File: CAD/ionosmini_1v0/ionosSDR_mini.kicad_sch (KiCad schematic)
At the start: 8 parts, among them CON1 TFC-120-02-F-D-A-K-TR, CON2 TFC-120-02-F-D-A-K-TR, IC1 ESP32-S3-DEVKITC-1-N8R2, SW1 PTS647SK38SMTR2 LFS, SW2 PTS647SK38SMTR2 LFS, SW3 PTS647SK38SMTR2 LFS, SW4 PTS647SK38SMTR2 LFS

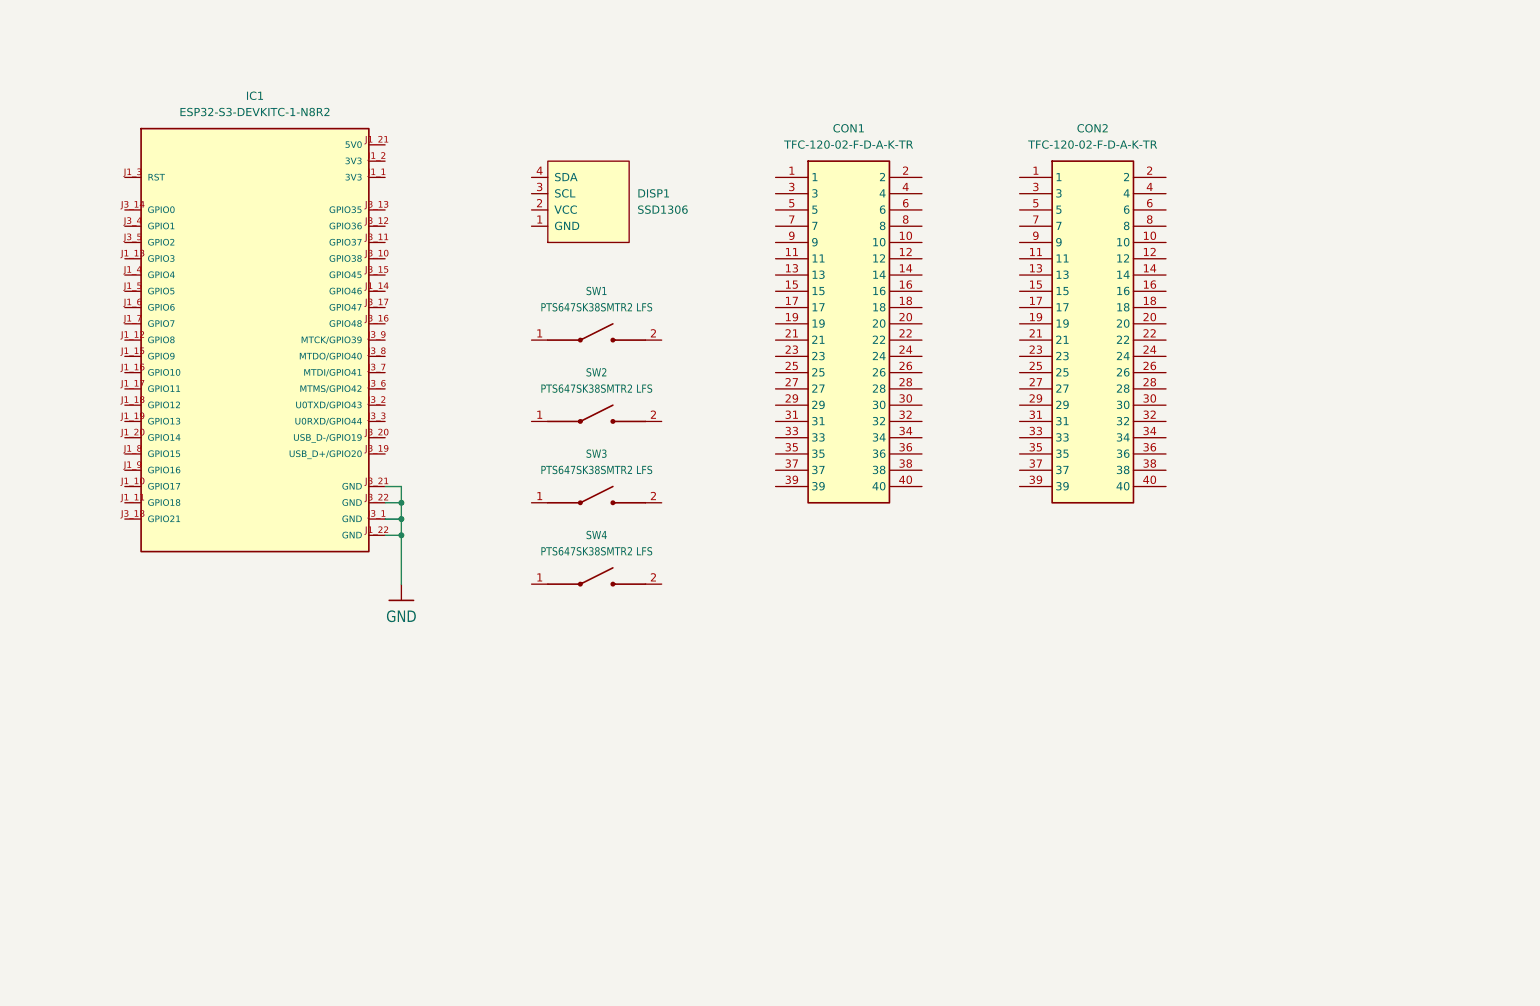
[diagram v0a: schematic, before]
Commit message: Pairing nets to ESP32
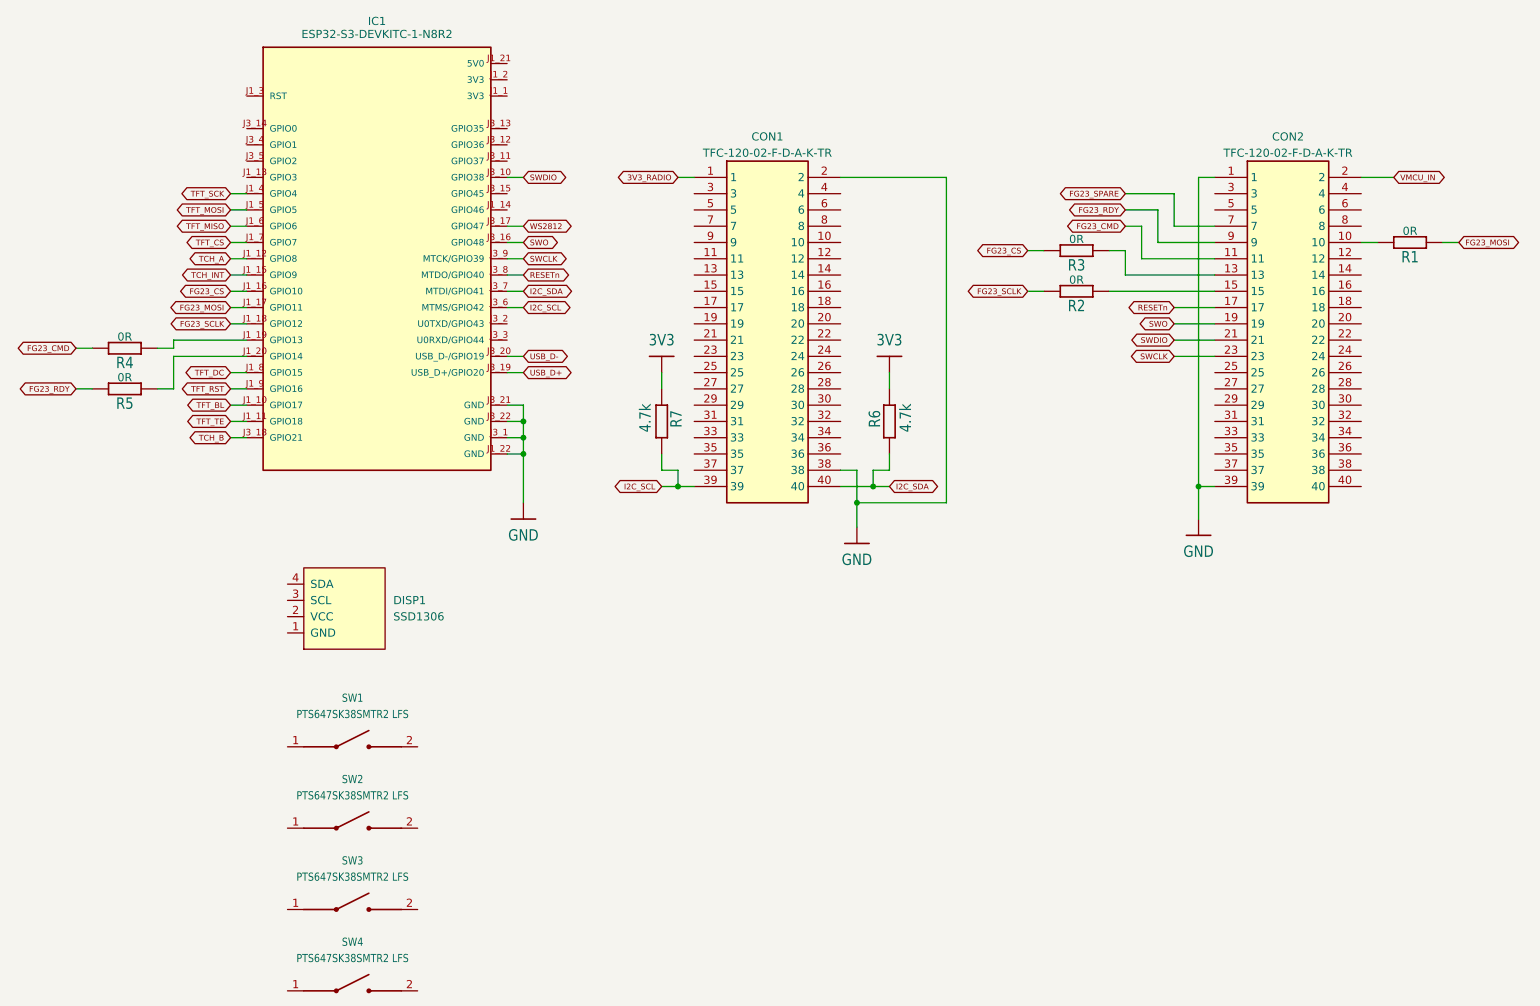
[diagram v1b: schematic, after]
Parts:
- added R1, R2, R3, R4, R5: 0R, rpw_lib:RESC1005X40_0402, symbol rpw_resistors:R_0R_JUMPER_0402(1005-METRIC)
- added R6, R7: 4.7k, rpw_lib:RESC1005X40_0402, symbol rpw_resistors:R_4.7K_5%_0402(1005-METRIC)
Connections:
- net GND: now also CON1.2, CON1.38, CON2.1, CON2.39
- net at CON2.10: now also R1.1
- net FG23_CMD: now reaches CON2.11
- net FG23_CMD: now also R4.1
- net at CON2.13: now also R3.2
- net at CON2.15: now also R2.2
- net RESETn: now reaches CON2.17
- net RESETn: now also IC1.J3_8 (MTDO/GPIO40)
- net SWO: now reaches CON2.19
- net SWO: now also IC1.J3_16 (GPIO48)
- net VMCU_IN: now reaches CON2.2
- net SWDIO: now reaches CON2.21
- net SWDIO: now also IC1.J3_10 (GPIO38)
- net SWCLK: now reaches CON2.23
- net SWCLK: now also IC1.J3_9 (MTCK/GPIO39)
- net FG23_SPARE: now reaches CON2.7
- net FG23_RDY: now reaches CON2.9
- net FG23_RDY: now also R5.1
- net 3V3_RADIO: now reaches CON1.1
- net I2C_SCL: now reaches CON1.39
- net I2C_SCL: now also IC1.J3_6 (MTMS/GPIO42), R7.1
- net I2C_SDA: now reaches CON1.40
- net I2C_SDA: now also IC1.J3_7 (MTDI/GPIO41), R6.1
- net TFT_BL: now reaches IC1.J1_10 (GPIO17)
- net TFT_TE: now reaches IC1.J1_11 (GPIO18)
- net TCH_A: now reaches IC1.J1_12 (GPIO8)
- net TCH_INT: now reaches IC1.J1_15 (GPIO9)
- net FG23_CS: now reaches IC1.J1_16 (GPIO10)
- net FG23_CS: now also R3.1
- net FG23_MOSI: now reaches IC1.J1_17 (GPIO11)
- net FG23_MOSI: now also R1.2
- net FG23_SCLK: now reaches IC1.J1_18 (GPIO12)
- net FG23_SCLK: now also R2.1
- net at IC1.J1_19 (GPIO13): now also R4.2
- net at IC1.J1_20 (GPIO14): now also R5.2
- net TFT_SCK: now reaches IC1.J1_4 (GPIO4)
- net TFT_MOSI: now reaches IC1.J1_5 (GPIO5)
- net TFT_MISO: now reaches IC1.J1_6 (GPIO6)
- net TFT_CS: now reaches IC1.J1_7 (GPIO7)
- net TFT_DC: now reaches IC1.J1_8 (GPIO15)
- net TFT_RST: now reaches IC1.J1_9 (GPIO16)
- net WS2812: now reaches IC1.J3_17 (GPIO47)
- net TCH_B: now reaches IC1.J3_18 (GPIO21)
- net USB_D+: now reaches IC1.J3_19 (USB_D+/GPIO20)
- net USB_D-: now reaches IC1.J3_20 (USB_D-/GPIO19)
- new net 3V3: R6.2, R7.2
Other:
- moved on the sheet: CON1, CON2, DISP1, IC1, SW1, SW2, SW3, SW4

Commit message: cad(ionosmini_1v0): schematic completed, 4-layer layout routed
Schematic
  - LP5907MFX-3.3 ultra-low-noise LDO for the radio-board rail (6.5 uVrms
    vs ~66 uVrms for the NCP176), fed from 5V0 through FB1
  - cuttable solder jumpers JP1..JP8 on every signal that leaves at the
    mezzanine, so a wrong connection can be cut and blue-wired; together
    with the existing series R1..R5 and R8 every exit point now has
    exactly one cut point
  - RESETn moved from CON2.17 to CON1.17 (WSTK_F4), TCH_INT/TCH_B swap
    corrected, SW1..SW4 labelled, PWR_FLAGs, no-connects on the unused
    connector pins
  - ER-TFTM024-3 cradle-side socket footprint added (new file)

Layout
  - 4 layers: F.Cu signal + GND pour / In1.Cu solid GND / In2.Cu signal /
    B.Cu solid GND.  Signals are kept off the two plane layers.
  - autorouted and then checked, 4683 mm of track, 90 routing vias
  - 82 GND stitching vias on a 200 mil (5.08 mm) raster
  - ERC 0 errors, DRC 0 violations, 0 schematic-parity issues

Mezzanine orientation
  The terminals were initially placed 180 degrees out: our pin n met the
  radio board's pin 41-n.  The pads line up perfectly either way - only
  the numbering reverses - so neither ERC, DRC nor a netlist check can
  see it.  With that placement 3V3_RADIO would have landed on
  BOARD_ID_SDA and VMCU_IN on GND, shorting the regulator.

  The correct orientation was established from the Silabs BRD4265B
  gerbers: alignment holes +/-13.651 mm about each connector centre and
  24.000 mm between the two (.DRL); pad raster 1.27 mm, u = 2.935..27.065,
  rows +/-1.45 mm (.GBL); the "40" legend at the high-u end on both
  connectors (.GBO), confirmed by the 40-pad copper pattern of P201
  matching its known connectivity bit for bit in that orientation and no
  other.  Cross-checked against the Samtec SFC-120-T2-L-D-A decal in
  Silabs' own WSTK adapter (WES0108-03) and against a physical WSTK
  mainboard, where pin 1 of both horizontal terminals is bottom-left -
  as it 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
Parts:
- added C1, C6: 10u, rpw_lib:CAPC1005X60_0402, symbol rpw_capacitors:C_10U_6.3V_0402(1005-METRIC)
- added C10, C4, C5, C7, C8, C9: 100n, rpw_lib:CAPC1005X60_0402, symbol rpw_capacitors:C_100N_50V_0402(1005-METRIC)
- added C2, C3: 1u, rpw_lib:CAPC1005X60_0402, symbol rpw_capacitors:C_1U_16V_0402(1005-METRIC)
- added DISP2: ER-TFTM024-3, ionosSDR_mini:ER-TFTM024-3_Socket_2x20_P2.54mm, symbol ionosSDR_mini:ER-TFTM024-3
- added FB1: 600R@100MHz, rpw_lib:L5_0603, symbol rpw_inductors:L5_FERRITE_BEAD/0603
- added H1, H2, H3, H4: M3, rpw_lib:PB_HOLE, symbol rpw_lib:PB_HOLE
- added JP1, JP2, JP3, JP4, JP5, JP6, JP7, JP8: (no value), Jumper:SolderJumper-2_P1.3mm_Bridged_RoundedPad1.0x1.5mm, symbol Jumper:SolderJumper_2_Bridged
- added R16, R22, R8: 0R, rpw_lib:RESC1005X40_0402, symbol rpw_resistors:R_0R_JUMPER_0402(1005-METRIC)
- added R17, R23: 2k2, rpw_lib:RESC1005X40_0402, symbol rpw_resistors:R_2K2_1%_0402(1005-METRIC)
- added R18: 6k8, rpw_lib:RESC1005X40_0402, symbol rpw_resistors:R_6.8K_1%_0402(1005-METRIC)
- added R19: 22k, rpw_lib:RESC1005X70_0402, symbol rpw_resistors:R_22K_1%_0402(1005-METRIC)
- added R20, R24, R9: 10k, rpw_lib:RESC1005X40_0402, symbol rpw_resistors:R_10K_1%_0402(1005-METRIC)
- added R21, R25: 1k, rpw_lib:RESC1005X40_0402, symbol rpw_resistors:R_1K_1%_0402(1005-METRIC)
- added R26, R27: 4k7 DNP, rpw_lib:RESC1005X40_0402, symbol rpw_resistors:R_4.7K_5%_0402(1005-METRIC)
- added SW5: BACK, rpw_lib:PTS647SK38SMTR2LFS, symbol rpw_lib:PTS647SK38SMTR2LFS
- added SW6: OK, rpw_lib:PTS647SK38SMTR2LFS, symbol rpw_lib:PTS647SK38SMTR2LFS
- added TP1: 5V0, rpw_lib:TESTPOINT_40MIL_SMD, symbol rpw_lib:TESTPOINT_40MIL_SMD
- added TP2: 3V3, rpw_lib:TESTPOINT_40MIL_SMD, symbol rpw_lib:TESTPOINT_40MIL_SMD
- added TP3: 3V3_RADIO, rpw_lib:TESTPOINT_40MIL_SMD, symbol rpw_lib:TESTPOINT_40MIL_SMD
- added TP4: VMCU_IN, rpw_lib:TESTPOINT_40MIL_SMD, symbol rpw_lib:TESTPOINT_40MIL_SMD
- added TP5: GND, rpw_lib:TESTPOINT_40MIL_SMD, symbol rpw_lib:TESTPOINT_40MIL_SMD
- added TP6: FG23_RDY, rpw_lib:TESTPOINT_40MIL_SMD, symbol rpw_lib:TESTPOINT_40MIL_SMD
- added TP7: FG23_CMD, rpw_lib:TESTPOINT_40MIL_SMD, symbol rpw_lib:TESTPOINT_40MIL_SMD
- added U1: LP5907MFX-3.3, rpw_lib:SOT-23-5, symbol ionosSDR_mini:LP5907MFX-3.3
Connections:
- net 3V3: now also DISP1.2 (VCC), IC1.J1_1 (3V3), IC1.J1_2 (3V3), C6.1, C7.1, DISP2.26 (/RD), R20.1, R24.1, R26.1, R27.1, TP2.PP
- net 3V3_RADIO: now also C3.1, C4.1, C8.1, JP1.1 (A), R8.1, TP3.PP, U1.5 (OUT); no longer CON1.1
- net FG23_CMD: now also TP7.PP
- net FG23_RDY: now also R9.1, TP6.PP
- net FG23_SPARE: now also JP5.1 (A); no longer CON2.7
- net GND: now also DISP1.1 (GND), SW1.2, SW2.2, SW3.2, SW4.2, C1.2, C10.2, C2.2, C3.2, C4.2, C5.2, C6.2, C7.2, C8.2, C9.2, DISP2.1 (VSS), DISP2.40 (VSS), R9.2, SW5.2, SW6.2, TP5.PP, U1.2 (GND)
- net I2C_SCL: now also DISP1.3 (SCL), JP3.1 (A), R26.2; no longer CON1.39, R7.1
- net I2C_SDA: now also DISP1.4 (SDA), JP4.1 (A), R27.2; no longer CON1.40, R6.1
- net RESETn: now also JP2.1 (A); no longer CON2.17
- net SWCLK: now also JP8.1 (A); no longer CON2.23
- net SWDIO: now also JP7.1 (A); no longer CON2.21
- net SWO: now also JP6.1 (A); no longer CON2.19
- net TCH_A: now also DISP2.30 (CTP_SCL)
- net TCH_B: now also IC1.J1_15 (GPIO9), DISP2.31 (CTP_SDA); no longer IC1.J3_18 (GPIO21)
- net TCH_INT: now also IC1.J3_18 (GPIO21), DISP2.39 (CTP_INT); no longer IC1.J1_15 (GPIO9)
- net TFT_BL: now also DISP2.29 (BL_ON/OFF)
- net TFT_CS: now also DISP2.23 (LCD_/CS)
- net TFT_DC: now also DISP2.25 (/WR(D/C))
- net TFT_MISO: now also DISP2.28 (LCD_SDO), DISP2.32 (SDO)
- net TFT_MOSI: now also DISP2.27 (LCD_SDI), DISP2.34 (SDI)
- net TFT_RST: now also DISP2.21 (/RESET_NC)
- net TFT_SCK: now also DISP2.24 (D/C(SCL)), DISP2.33 (SCL)
- net TFT_TE: now also DISP2.22 (TE)
- net VMCU_IN: now also C5.1, R8.2, TP4.PP
- net BTN_B1: now reaches SW1.1
- net BTN_B1: now also R16.2
- net BTN_B2: now reaches SW2.1
- net BTN_B2: now also R17.2
- net RESETn_RB: now reaches CON1.17
- net RESETn_RB: now also JP2.2 (B)
- net BTN_B3: now reaches SW3.1
- net BTN_B3: now also R18.2
- net BTN_B4: now reaches SW4.1
- net BTN_B4: now also R19.2
- net 5V0: now reaches IC1.J1_21 (5V0)
- net 5V0: now also C1.1, DISP2.2 (VDD), FB1.1 (P$1), TP1.PP
- net BTN_A: now reaches IC1.J3_4 (GPIO1)
- net BTN_A: now also C10.1, R25.2
- net BTN_B: now reaches IC1.J3_5 (GPIO2)
- net BTN_B: now also C9.1, R21.2
- new net 3V3_RADIO_RB: CON1.1, JP1.2 (B)
- new net 5V_LDO: C2.1, FB1.2 (P$2), U1.1 (IN), U1.3 (EN)
- new net BTN_A1: R22.2, SW5.1
- new net BTN_A2: R23.2, SW6.1
- new net BTN_A_RAW: R22.1, R23.1, R24.2, R25.1
- new net BTN_B_RAW: R16.1, R17.1, R18.1, R19.1, R20.2, R21.1
- new net FG23_SPARE_RB: CON2.7, JP5.2 (B)
- new net I2C_SCL_RB: CON1.39, JP3.2 (B), R7.1
- new net I2C_SDA_RB: CON1.40, JP4.2 (B), R6.1
- new net SWCLK_RB: CON2.23, JP8.2 (B)
- new net SWDIO_RB: CON2.21, JP7.2 (B)
- new net SWO_RB: CON2.19, JP6.2 (B)
- no-connect marks 0 -> 95
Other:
- note added: "BUTTONS two ADC ladders on GPIO1 / GPIO2"
- note added: "CUT-POINTS one solder jumper per radio-board signal"
- note added: "ERC power-source markers"
- note added: "GPIO35/36/37 are used by the octal PSRAM on the N16R8 module - do not route"
- note added: "MOUNTING"
- note added: "POWER 5V -> ferrite -> LP5907 -> 3V3_RADIO -> VMCU_IN"
- note added: "TEST POINTS"
- note added: "TFT ER-TFTM024-3 2x20 4-wire SPI, 5V"

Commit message: schematic v2: hierarchical Olimex-style redesign, pin map v2
Root sheet plus power / radio / ui sheets on A3. Supplies and GND are
symbols, labels only on pin stubs, 1.27 mm grid, no wire through a body,
values in Olimex format, not-fitted parts as NA(value). The DevKit symbol
is split into four units (power, radio link, user interface, reserved).

Pin map v2 (claude/ionos-mini-pinmap-v2-2026-10-09.md):
- TCH_B = GPIO21 (header 31), TCH_INT = GPIO9 (header 39)
- 10k pull-ups to 3V3 on display header 35/36/37 (SD_CS, FONT_CS,
  FLASH_CS), R28-R30; 4.7k pull-ups on TCH_A/TCH_B, R31/R32
- 10uF + 100nF at the TFT VDD (C11, C12)
- P201-40 VRF_IN to test point TP8 only; P200-37 5V_RADIO via a
  not-fitted 0R (R33) from the DevKit 5 V
- BTN_A ladder: BACK 0R, OK 2k2, SPARE 6k8 (R34, SW7 optional key),
  the same 0R/2k2/6k8/22k set as BTN_B, one firmware threshold table

twin: schstyle/lint.py checks rules L1-L15 on the sheets (--selftest
injects one fault per rule, 14/14 caught); twin_check asserts every
pin map v2 item; twin_plug accepts an open radio-board pin that only
runs to a test point (VRF_IN, WARN instead of FAIL).

ERC 0 errors. Schematic PDF in docs/.
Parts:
- removed C1, C6: 10u, rpw_lib:CAPC1005X60_0402, symbol rpw_capacitors:C_10U_6.3V_0402(1005-METRIC)
- removed C10, C4, C5, C7, C8, C9: 100n, rpw_lib:CAPC1005X60_0402, symbol rpw_capacitors:C_100N_50V_0402(1005-METRIC)
- removed C2, C3: 1u, rpw_lib:CAPC1005X60_0402, symbol rpw_capacitors:C_1U_16V_0402(1005-METRIC)
- removed CON1, CON2: TFC-120-02-F-D-A-K-TR, ionosSDR_mini:TFC-120-02-XX-D-A-K-TR, symbol ionosSDR_mini:TFC-120-02-F-D-A-K-TR
- removed DISP1: SSD1306, ionosSDR_mini:128x64OLED, symbol ionosSDR_mini:SSD1306
- removed DISP2: ER-TFTM024-3, ionosSDR_mini:ER-TFTM024-3_Socket_2x20_P2.54mm, symbol ionosSDR_mini:ER-TFTM024-3
- removed FB1: 600R@100MHz, rpw_lib:L5_0603, symbol rpw_inductors:L5_FERRITE_BEAD/0603
- removed IC1: ESP32-S3-DEVKITC-1-N8R2, ionosSDR_mini:XCVR_ESP32-S3-DEVKITC-1-N8R2, symbol ionosSDR_mini:ESP32-S3-DEVKITC-1-N8R2
- removed JP1, JP2, JP3, JP4, JP5, JP6, JP7, JP8: (no value), Jumper:SolderJumper-2_P1.3mm_Bridged_RoundedPad1.0x1.5mm, symbol Jumper:SolderJumper_2_Bridged
- removed R1, R16, R2, R22, R3, R4, R5, R8: 0R, rpw_lib:RESC1005X40_0402, symbol rpw_resistors:R_0R_JUMPER_0402(1005-METRIC)
- removed R17, R23: 2k2, rpw_lib:RESC1005X40_0402, symbol rpw_resistors:R_2K2_1%_0402(1005-METRIC)
- removed R18: 6k8, rpw_lib:RESC1005X40_0402, symbol rpw_resistors:R_6.8K_1%_0402(1005-METRIC)
- removed R19: 22k, rpw_lib:RESC1005X70_0402, symbol rpw_resistors:R_22K_1%_0402(1005-METRIC)
- removed R20, R24, R9: 10k, rpw_lib:RESC1005X40_0402, symbol rpw_resistors:R_10K_1%_0402(1005-METRIC)
- removed R21, R25: 1k, rpw_lib:RESC1005X40_0402, symbol rpw_resistors:R_1K_1%_0402(1005-METRIC)
- removed R26, R27: 4k7 DNP, rpw_lib:RESC1005X40_0402, symbol rpw_resistors:R_4.7K_5%_0402(1005-METRIC)
- removed R6, R7: 4.7k, rpw_lib:RESC1005X40_0402, symbol rpw_resistors:R_4.7K_5%_0402(1005-METRIC)
- removed SW1, SW2, SW3, SW4: PTS647SK38SMTR2 LFS, rpw_lib:PTS647SK38SMTR2LFS, symbol rpw_lib:PTS647SK38SMTR2LFS
- removed SW5: BACK, rpw_lib:PTS647SK38SMTR2LFS, symbol rpw_lib:PTS647SK38SMTR2LFS
- removed SW6: OK, rpw_lib:PTS647SK38SMTR2LFS, symbol rpw_lib:PTS647SK38SMTR2LFS
- removed TP1: 5V0, rpw_lib:TESTPOINT_40MIL_SMD, symbol rpw_lib:TESTPOINT_40MIL_SMD
- removed TP2: 3V3, rpw_lib:TESTPOINT_40MIL_SMD, symbol rpw_lib:TESTPOINT_40MIL_SMD
- removed TP3: 3V3_RADIO, rpw_lib:TESTPOINT_40MIL_SMD, symbol rpw_lib:TESTPOINT_40MIL_SMD
- removed TP4: VMCU_IN, rpw_lib:TESTPOINT_40MIL_SMD, symbol rpw_lib:TESTPOINT_40MIL_SMD
- removed TP5: GND, rpw_lib:TESTPOINT_40MIL_SMD, symbol rpw_lib:TESTPOINT_40MIL_SMD
- removed TP6: FG23_RDY, rpw_lib:TESTPOINT_40MIL_SMD, symbol rpw_lib:TESTPOINT_40MIL_SMD
- removed TP7: FG23_CMD, rpw_lib:TESTPOINT_40MIL_SMD, symbol rpw_lib:TESTPOINT_40MIL_SMD
- removed U1: LP5907MFX-3.3, rpw_lib:SOT-23-5, symbol ionosSDR_mini:LP5907MFX-3.3
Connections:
- no-connect marks 95 -> 0
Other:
- added sheet Power and ESP32-S3 DevKit (power.kicad_sch)
- added sheet Radio board (BRD4265B) (radio.kicad_sch)
- added sheet User interface (ui.kicad_sch)
- note added: "3V3_RADIO, VMCU_IN"
- note added: "5V0 -> FB1 -> LP5907 -> 3V3_RADIO -> VMCU_IN"
- note added: "5V0, 3V3"
- note added: "A label sits on a short stub at a pin end; wires stay inside a block; supplies only as rail symbols."
- note added: "Assembly: R26/R27 DNP, value NA(4.7k). Values carry the critical parameter (value/voltage/tolerance)."
- note added: "Block diagram"
- note added: "Cut points JP1-JP8 isolate every radio-board signal; R1-R5 are 0R links on a damping-resistor footprint."
- note added: "Design notes"
- note added: "DevKit 3V3 decoupling, test points"
- note added: "ER-TFTM024-3 TFT, 4-wire SPI + XPT2046 touch"
- note added: "ESP32-S3 DevKitC-1 (N16R8): supply pins, reserved GPIO"
- note added: "FB1: value 600R@100MHz but MPN field BLM18SP300SH1D (30R) - resolve before ordering."
- note added: "FG23 SPI (IO_MUX slave) + UART + RDY"
- note added: "Forbidden: strapping 0/3/45/46, octal PSRAM 35-37 (N16R8). Reserved: UART0 43/44, USB 19/20, WS2812 47."
- note added: "GPIO plan: FG23 link on the SPI2 IO_MUX pins 10/11/12 + UART TX 13 + RDY 14; TFT on SPI3 via the"
- note added: "I2C_SDA/SCL (OLED shares the bus)"
- note added: "IC1A supply (p2), IC1B radio link (p3), IC1C user interface (p4), IC1D reserved (p2)."
- note added: "M3 mounting holes, not plated to GND"
- note added: "Mechanical"
- note added: "Net names are global (labels and rail symbols): layout, twin and firmware share one name per net."
- note added: "P200/P201 to the BRD4265B (EFR32FG23)"
- note added: "SSD1306 OLED on I2C 0x3C"
- note added: "SWD bit-bang, I2C board-ID, cut points JP1-JP8"
- note added: "The ESP32 module is split in four units, each on the page it serves:"
- note added: "matrix (4-7, 15-18); touch 8/9/21; buttons ADC1 1/2; I2C 41/42; SWD 38/39/48, RESETn 40."
- note added: "sheet symbols open the pages; arrows are the interfaces between them"
- note added: "two ADC1 button ladders (6 keys)"
- note removed: "BUTTONS two ADC ladders on GPIO1 / GPIO2"
- note removed: "CUT-POINTS one solder jumper per radio-board signal"
- note removed: "ERC power-source markers"
- note removed: "GPIO35/36/37 are used by the octal PSRAM on the N16R8 module - do not route"
- note removed: "MOUNTING"
- note removed: "POWER 5V -> ferrite -> LP5907 -> 3V3_RADIO -> VMCU_IN"
- note removed: "TEST POINTS"
- note removed: "TFT ER-TFTM024-3 2x20 4-wire SPI, 5V"
- company: (none) -> RF Sparkling Kft. - HA7DCD
- title: (none) -> ionos-sdr-mini rev-B3 - Overview
- moved on the sheet: H1, H2, H3, H4
